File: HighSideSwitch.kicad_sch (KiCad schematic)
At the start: 24 parts, among them J1 Conn_02x02_Odd_Even, Q1 CSD18540Q5B, Q2 CSD18540Q5B, Q3 8050, U1 LM5060, U2 LM5050-1

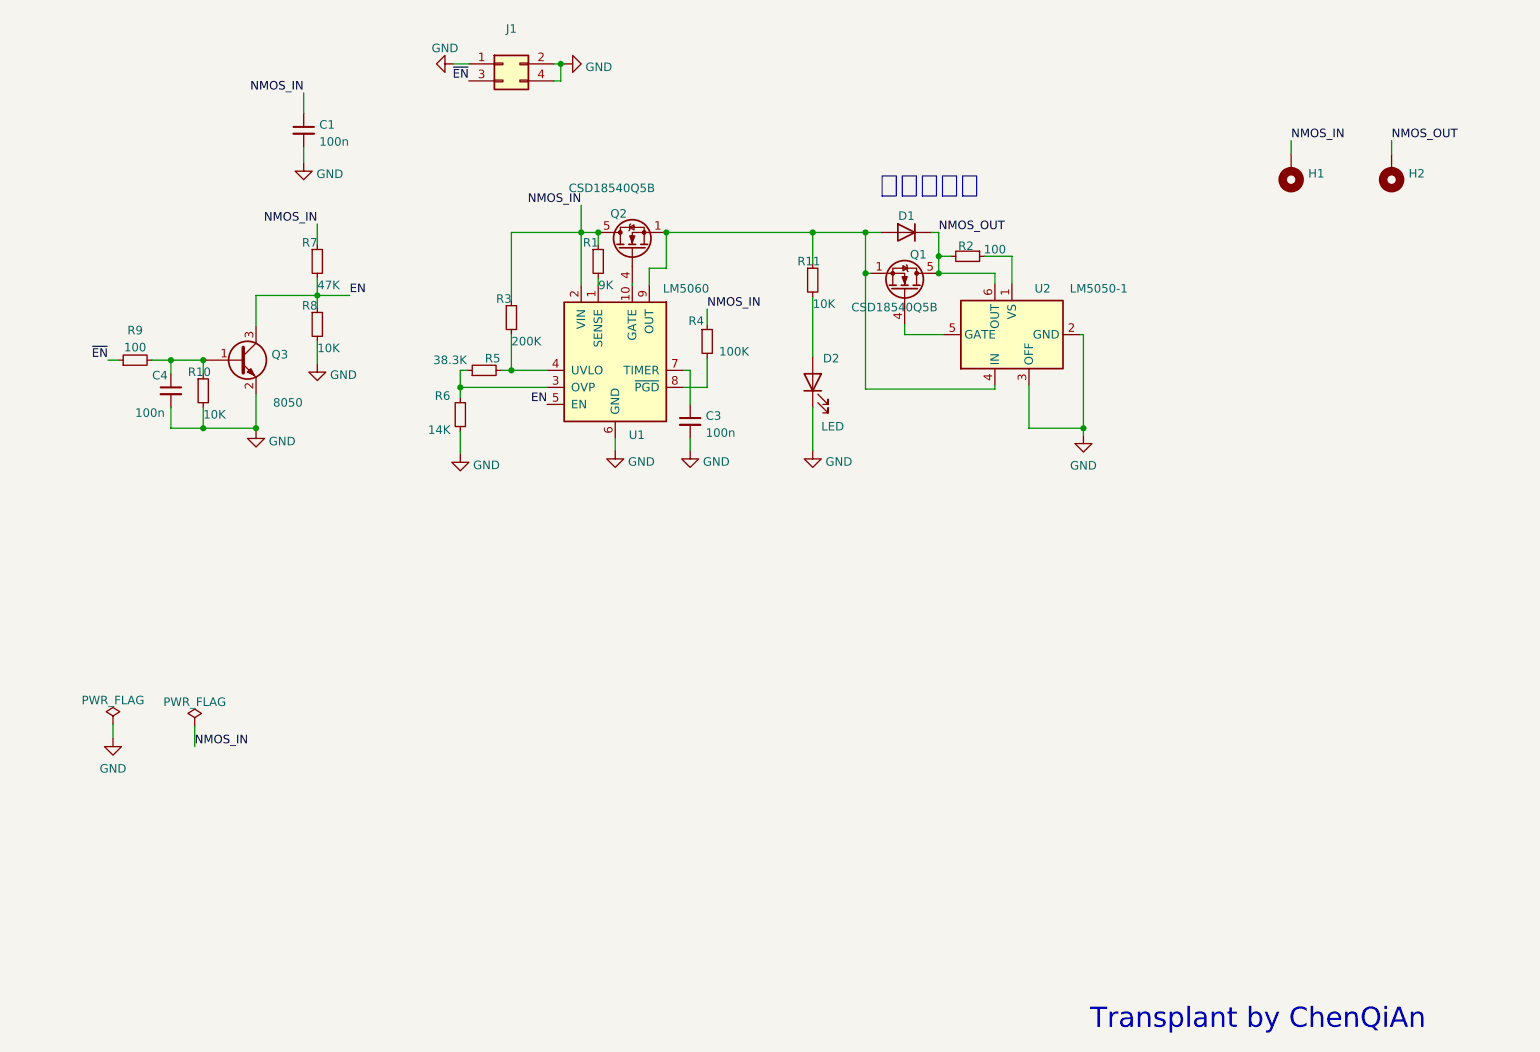
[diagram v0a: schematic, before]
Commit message: Transplant from old library to new one & change some routings & change some footprints from 0402 to 0603 & add teardrops
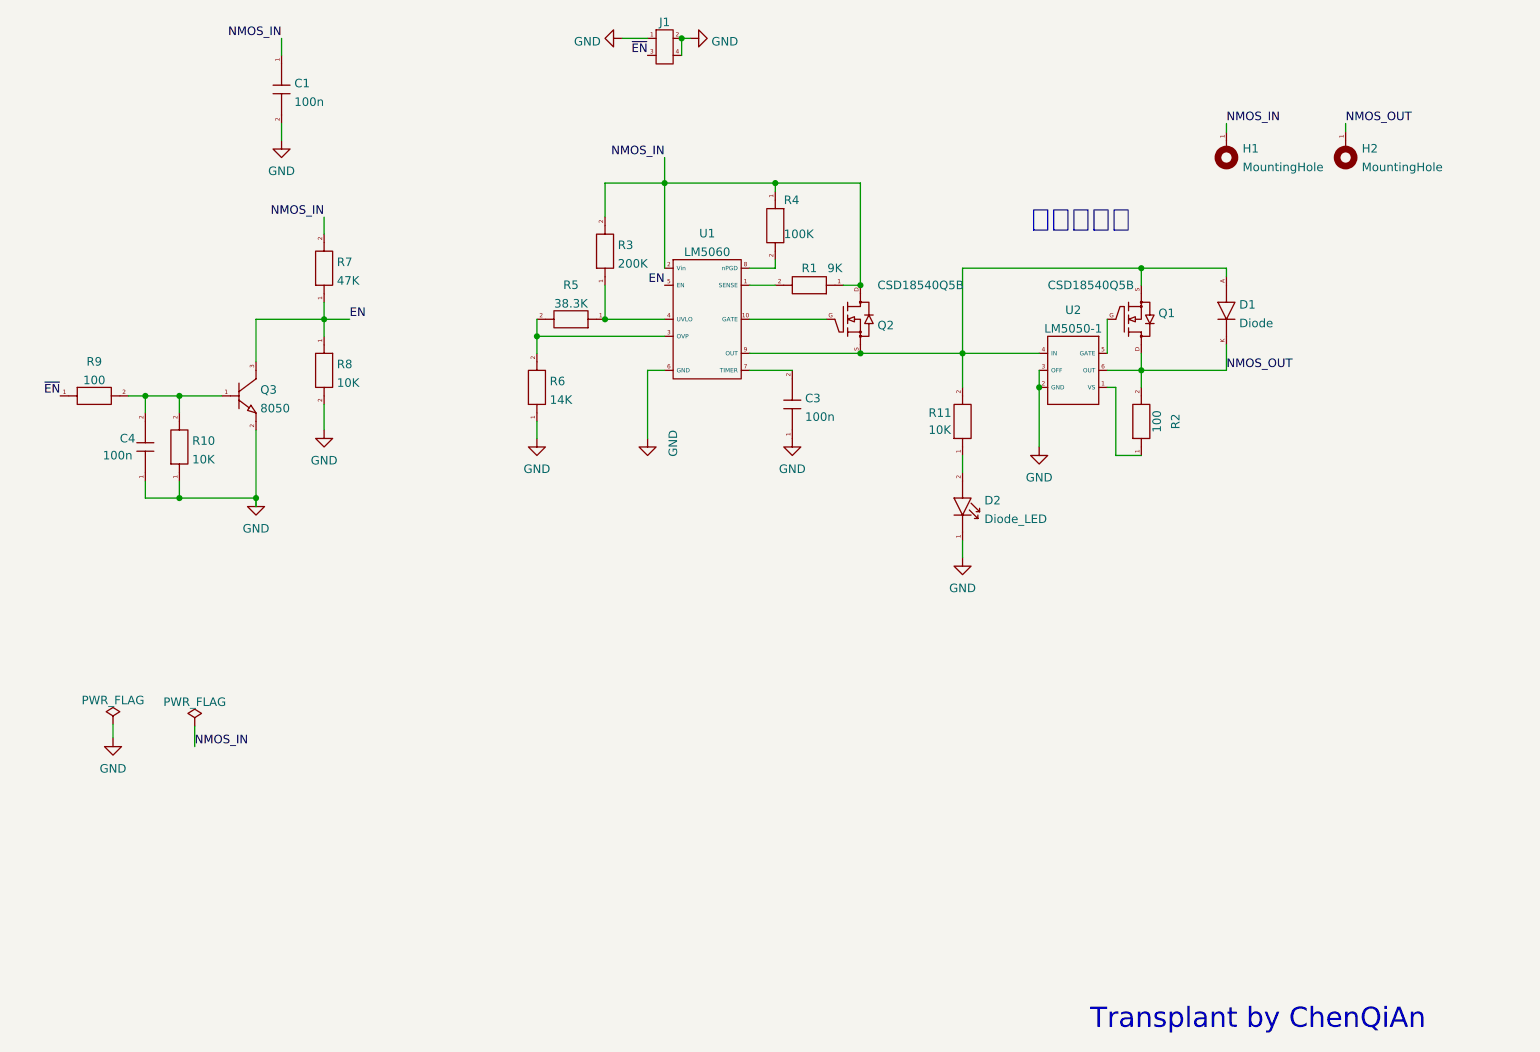
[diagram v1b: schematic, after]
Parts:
- removed C1, C3, C4: 100n, Capacitor_SMD:C_0402_1005Metric, symbol Device:C_Small
- removed D1: VS-6ESU06, Package_TO_SOT_SMD:TO-277A, symbol Diode:VS-6ESU06
- removed D2: LED, LED_SMD:LED_0603_1608Metric, symbol Device:LED
- removed H1, H2: MountingHole_Pad, MountingHole:MountingHole_3.2mm_M3_Pad_Via, symbol Mechanical:MountingHole_Pad
- removed J1: Conn_02x02_Odd_Even, Connector_PinHeader_1.27mm:PinHeader_2x02_P1.27mm_Vertical_SMD, symbol Connector_Generic:Conn_02x02_Odd_Even
- removed Q1, Q2: CSD18540Q5B, Package_TO_SOT_SMD:TDSON-8-1, symbol Transistor_FET:CSD18540Q5B
- removed Q3: 8050, Package_TO_SOT_SMD:TSOT-23, symbol Device:Q_NPN_BEC
- removed R1: 9K, Resistor_SMD:R_0402_1005Metric, symbol Device:R_Small
- removed R10, R11, R8: 10K, Resistor_SMD:R_0402_1005Metric, symbol Device:R_Small
- removed R2, R9: 100, Resistor_SMD:R_0402_1005Metric, symbol Device:R_Small
- removed R3: 200K, Resistor_SMD:R_0402_1005Metric, symbol Device:R_Small
- removed R4: 100K, Resistor_SMD:R_0402_1005Metric, symbol Device:R_Small
- removed R5: 38.3K, Resistor_SMD:R_0402_1005Metric, symbol Device:R_Small
- removed R6: 14K, Resistor_SMD:R_0402_1005Metric, symbol Device:R_Small
- removed R7: 47K, Resistor_SMD:R_0402_1005Metric, symbol Device:R_Small
- removed U1: LM5060, Package_SO:MSOP-10_3x3mm_P0.5mm, symbol Power_Management:LM5060
- removed U2: LM5050-1, Package_TO_SOT_SMD:TSOT-23-6, symbol Power_Management:LM5050-1
- added C1: 100n, GENERAL_RCL_SMD:C0402(1005M), symbol Basic_passive_components:Capacitor
- added C3, C4: 100n, GENERAL_RCL_SMD:C0603(1608M), symbol Basic_passive_components:Capacitor
- added D1: Diode, POWER_DIODE_SMD:TO-277A, symbol Power_diode:Diode
- added D2: Diode_LED, GENERAL_2-PIN_PLASTIC_SMD:LED0603(1608M), symbol Basic_semiconductor:Diode_LED
- added H1, H2: MountingHole, MountingHole:mountinghole, symbol MountingHole:MountingHole
- added J1: Conn_02x02, CONNECTOR_Odd_Even:Conn_02x02, symbol Link_W2B_connector:Conn_02x02
- added Q1, Q2: CSD18540Q5B, POWER_TRANSISTOR_SMD:SON-6050-FET, symbol Power_transistor:CSD18540Q5B
- added Q3: 8050, GENERAL_SMALL-SEMI_SMD:SOT-23, symbol Basic_semiconductor:BJT_NPN
- added R1: 9K, GENERAL_RCL_SMD:R0402(1005M), symbol Basic_passive_components:Resistor
- added R10, R11, R8: 10K, GENERAL_RCL_SMD:R0603(1608M), symbol Basic_passive_components:Resistor
- added R2, R9: 100, GENERAL_RCL_SMD:R0603(1608M), symbol Basic_passive_components:Resistor
- added R3: 200K, GENERAL_RCL_SMD:R0603(1608M), symbol Basic_passive_components:Resistor
- added R4: 100K, GENERAL_RCL_SMD:R0603(1608M), symbol Basic_passive_components:Resistor
- added R5: 38.3K, GENERAL_RCL_SMD:R0603(1608M), symbol Basic_passive_components:Resistor
- added R6: 14K, GENERAL_RCL_SMD:R0603(1608M), symbol Basic_passive_components:Resistor
- added R7: 47K, GENERAL_RCL_SMD:R0402(1005M), symbol Basic_passive_components:Resistor
- added U1: LM5060, GENERAL_MIDDLE-SEMI_SMD:MSOP-3030_10, symbol Integrated-circuit_transistor_driver:LM5060
- added U2: LM5050-1, GENERAL_SMALL-SEMI_SMD:SOT-23-6, symbol Integrated-circuit_transistor_driver:LM5050-1
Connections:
- net EN: now also Q3.3 (Collector), R7.1, R8.1, U1.5 (EN)
- net GND: now also C1.2, C3.1, C4.1, D2.1 (Cathode), J1.1, J1.2, J1.4, Q3.2 (Emitter), R10.1, R6.1, R8.2, U1.6 (GND), U2.2 (GND), U2.3 (OFF)
- net NMOS_IN: now also C1.1, H1.1, Q2.D (Drain), R1.1, R3.2, R4.1, R7.2, U1.2 (Vin)
- net NMOS_OUT: now also D1.K (Cathode), H2.1, Q1.D (Drain), R2.2, U2.6 (OUT)
- net ~{EN}: now also J1.3, R9.1
- new net: D1.A (Anode), Q1.S (Source), Q2.S (Source), R11.2, U1.9 (OUT), U2.4 (IN)
- new net: R2.1, U2.1 (VS)
- new net: Q1.G (Gate), U2.5 (GATE)
- new net: R4.2, U1.8 (nPGD)
- new net: C4.2, Q3.1 (Base), R10.2, R9.2
- new net: R1.2, U1.1 (SENSE)
- new net: Q2.G (Gate), U1.10 (GATE)
- new net: R5.2, R6.2, U1.3 (OVP)
- new net: R3.1, R5.1, U1.4 (UVLO)
- new net: C3.2, U1.7 (TIMER)
- new net: D2.2 (Anode), R11.1
